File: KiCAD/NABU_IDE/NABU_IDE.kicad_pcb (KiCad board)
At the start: 2 copper layers, 101.3 x 71.1 mm, 34 parts, among them J1 IDE ATA Bus, J2 NABU Expansion Header, J3 NABU Daisy Chain In, J4 NABU Daisy Chain Out, J5 NABU External Power, U1 74LS245, U2 74LS32, U3 74LS08, U4 74LS04, U5 74LS32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

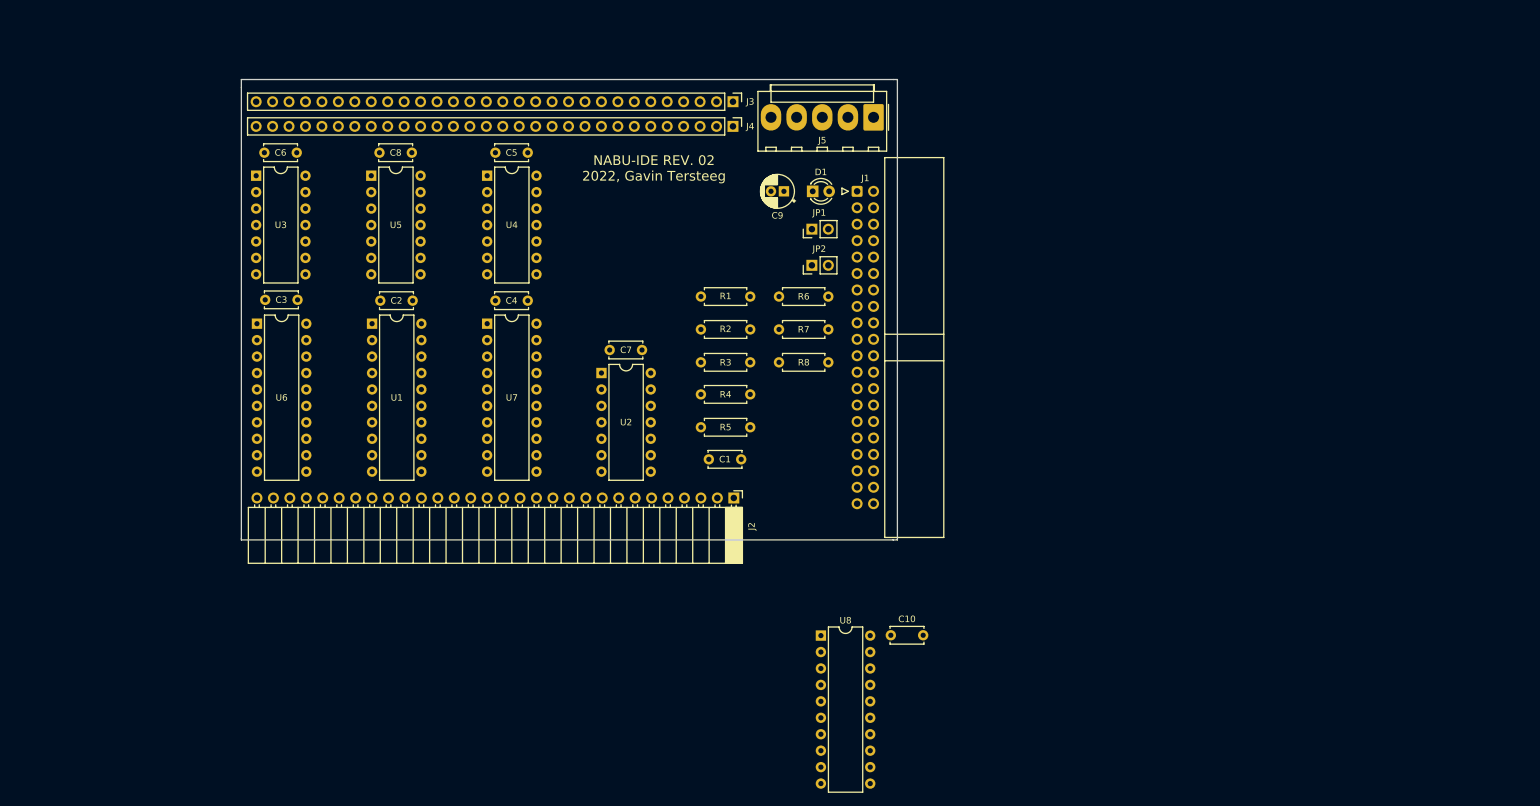
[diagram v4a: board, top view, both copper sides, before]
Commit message: Finished routing board and added mounting holes
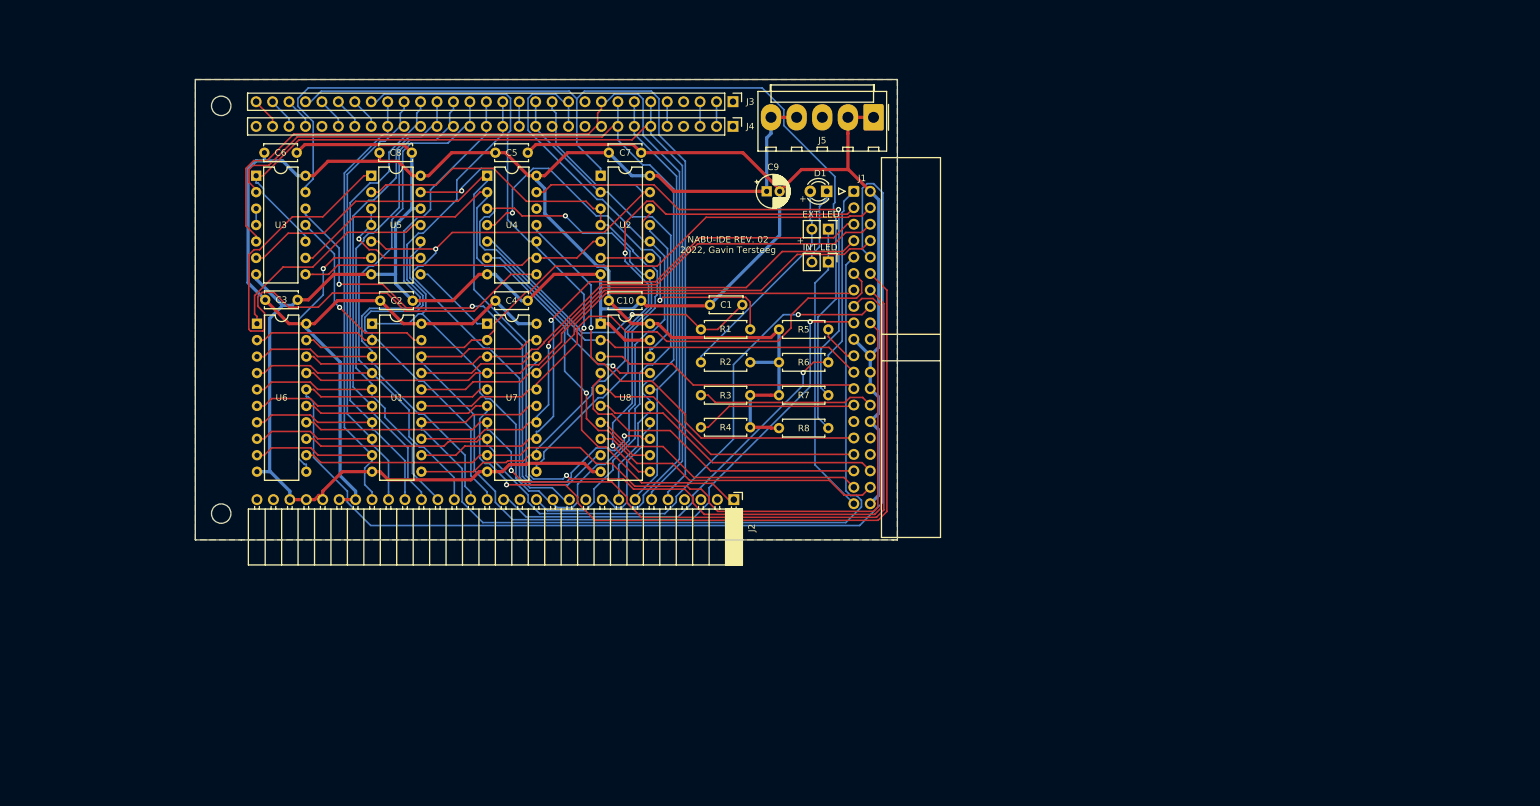
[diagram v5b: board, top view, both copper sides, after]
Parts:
- added H1: MountingHole, MountingHole:MountingHole_3mm, F.Cu at (63.8, 123.8)
- added H2: MountingHole, MountingHole:MountingHole_3mm, F.Cu at (63.8, 60.8)
- moved C10 67.6 mm to (123.7, 90.9)
- moved U8 59.0 mm to (122.4, 94.5)
- moved C7 30.5 mm to (123.7, 68.1)
- moved U2 30.5 mm to (122.4, 71.6)
- moved C1 23.9 mm to (139.3, 91.6)
- moved R5 15.8 mm to (150.0, 95.4), turned to 0 degrees
- moved R7 10.2 mm to (157.6, 105.5)
- moved R8 10.2 mm to (157.6, 110.6)
- moved R6 10.2 mm to (150.0, 100.5)
- moved R3 5.08 mm to (145.5, 105.5)
- moved R1 5.08 mm to (137.9, 95.4)
- moved R2 5.08 mm to (145.5, 100.5)
- moved R4 5.08 mm to (145.5, 110.5)
- moved C9 2.67 mm to (148.1, 74.0), turned to 0 degrees
- moved JP2 2.59 mm to (157.6, 85.0), turned to 270 degrees
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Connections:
- C9 pad 1: GND -> /+5V
- C9 pad 2: /+5V -> GND
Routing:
- net GND: track 0.00 -> 374.8 mm
- net /+5V: track 0.00 -> 294.3 mm
- net /IDE_D11: track 0.00 -> 197.8 mm
- net /NABU_A3: track 0.00 -> 170.0 mm
- net /*NABU_RD: track 0.00 -> 155.3 mm
- net Net-(R8-Pad1): track 0.00 -> 147.6 mm
- net /IDE_D12: track 0.00 -> 143.6 mm, vias 0 -> 1
- net /NABU_A0: track 0.00 -> 143.1 mm
- net /BUF_D4: track 0.00 -> 138.5 mm
- net /*NABU_CS: track 0.00 -> 134.9 mm
- net /NABU_A2: track 0.00 -> 134.4 mm
- net /IDE_D13: track 0.00 -> 134.4 mm, vias 0 -> 1
- net /BUF_D1: track 0.00 -> 132.2 mm, vias 0 -> 1
- net /*NABU_WR: track 0.00 -> 125.7 mm, vias 0 -> 1
- net /IDE_D15: track 0.00 -> 123.5 mm
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- added copper zone on B.Cu, net GND
- added copper zone on F.Cu, net GND
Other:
- board size 101.3 x 71.1 mm -> 108.5 x 71.1 mm
- board text added: "+"
- board text added: "EXT LED"
- board text added: "INT LED"

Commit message: Added gerbers and made some silkscreen changes
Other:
- board text added: "JLCJLCJLCJLC"
